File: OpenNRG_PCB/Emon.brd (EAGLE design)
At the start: 74.9 x 52.8 mm, 63 parts, among them J1 POWER_JACKSMD, Q4 16000, U1 ATMEGA368

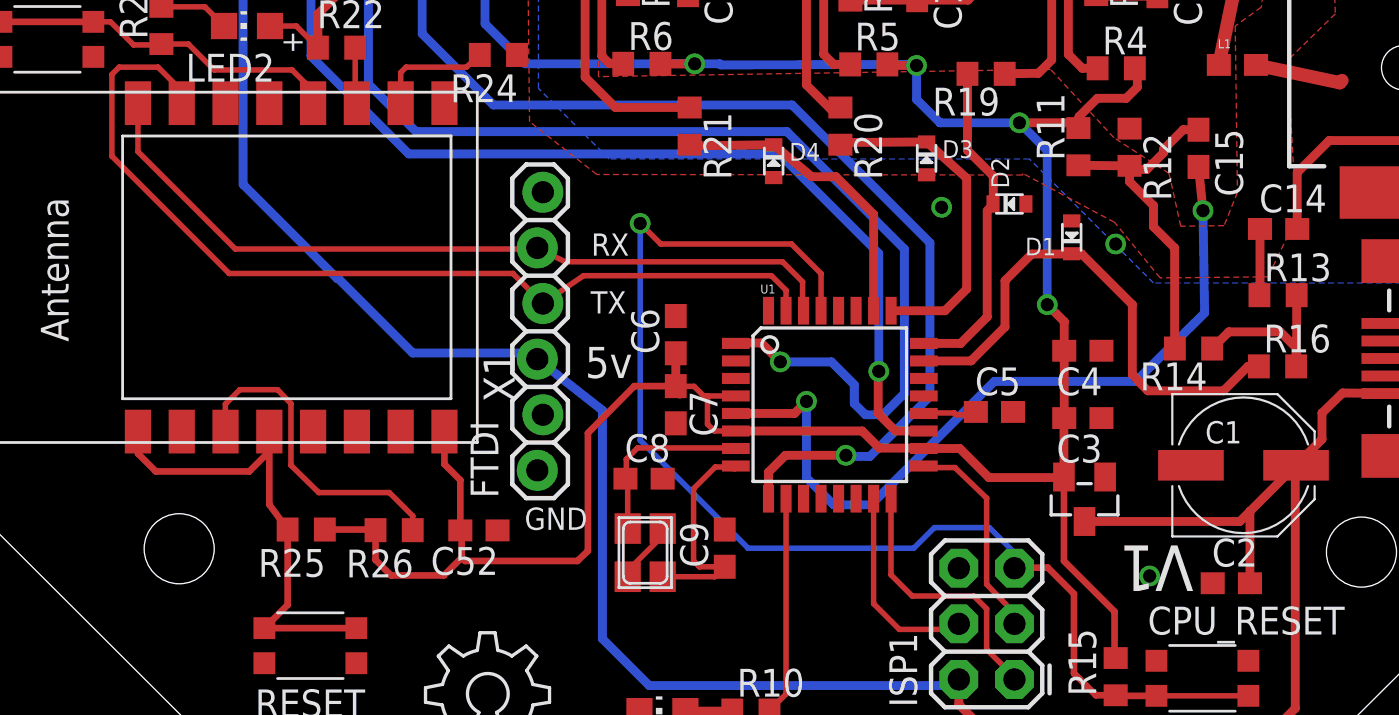
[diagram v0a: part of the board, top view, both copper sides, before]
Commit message: Re-write or ESP code and updated to board files
Update to ESP8266 firmware to support latest board manager.
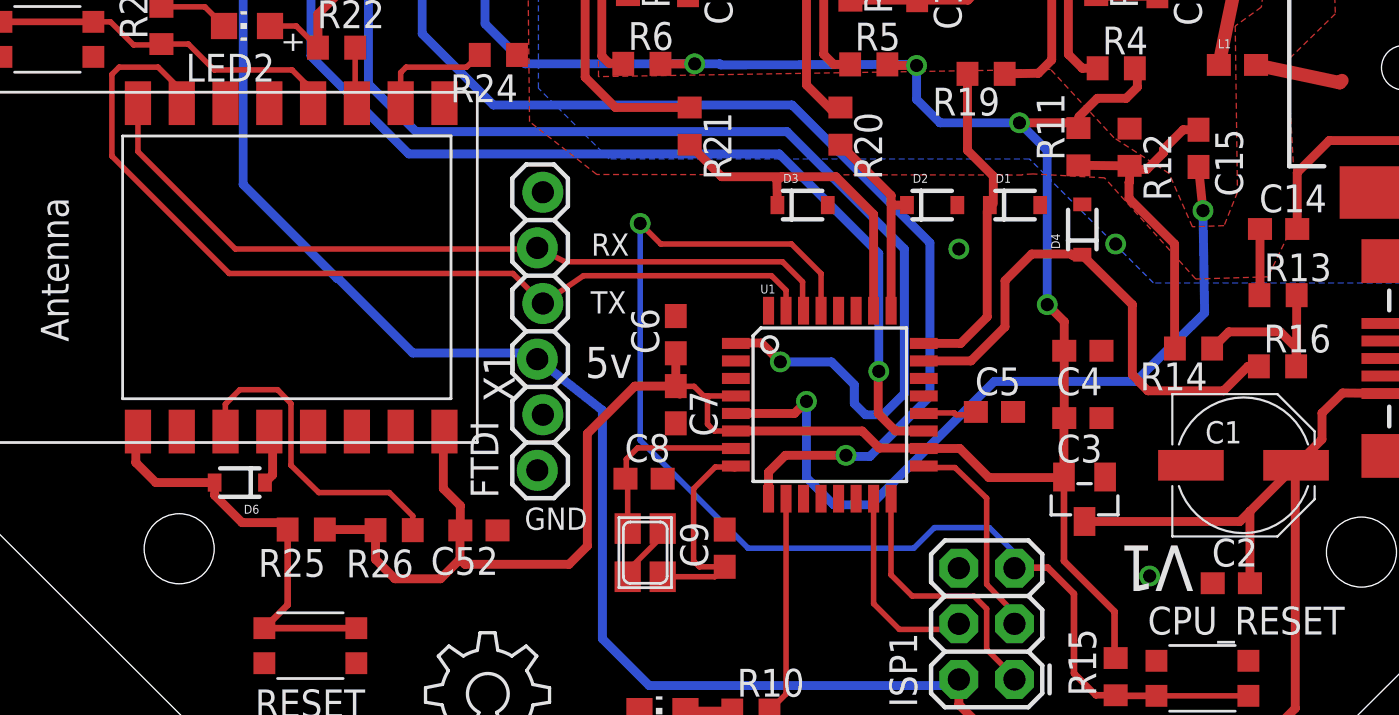
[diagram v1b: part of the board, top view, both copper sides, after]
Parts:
- added D6: (no value), SparkFun:SOD-323
- D1: value (none) -> 5.1v; device microbuilder:SOD-523 -> SparkFun:SOD-323
- D2, D4: value (none) -> 5.1; device microbuilder:SOD-523 -> SparkFun:SOD-323
- D3: value GND -> 5.1; device microbuilder:SOD-523 -> SparkFun:SOD-323
- moved D4 14.4 mm to (51.7, 25.2), turned to 90 degrees
- moved D3 6.05 mm to (38.9, 26.3)
- moved D2 3.53 mm to (44.9, 26.3), turned to 0 degrees
- moved D1 2.98 mm to (48.6, 26.3), turned to 0 degrees
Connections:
- new net N$12: D6.1, X1.4
- net ADC0: now also D4.1; no longer D1.K
- net ADC1: now also D1.1; no longer D2.K
- net ADC2: now also D2.1; no longer D3.K
- net ADC3: now also D3.1; no longer D4.K
- net GND: now also D1.2, D2.2, D3.2, D4.2; no longer D1.A, D2.A, D3.A, D4.A
- net N$15: now also D6.2; no longer X1.4
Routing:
- net ADC2: track 15.4 -> 9.44 mm
- net N$12: track 0.00 -> 2.54 mm
- net N$15: track 21.7 -> 19.8 mm
- net ADC3: track 14.1 -> 15.6 mm
